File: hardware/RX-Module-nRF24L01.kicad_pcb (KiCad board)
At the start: 2 copper layers, 50 x 22.9 mm, 33 parts, among them J1 Conn_01x03, J10 Conn_01x03, J11 Conn_01x03, J2 Conn_01x03, J3 Conn_01x03, J4 Conn_01x03, J5 Conn_01x03, J6 Conn_01x03, J7 Conn_01x03, J8 Conn_01x03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

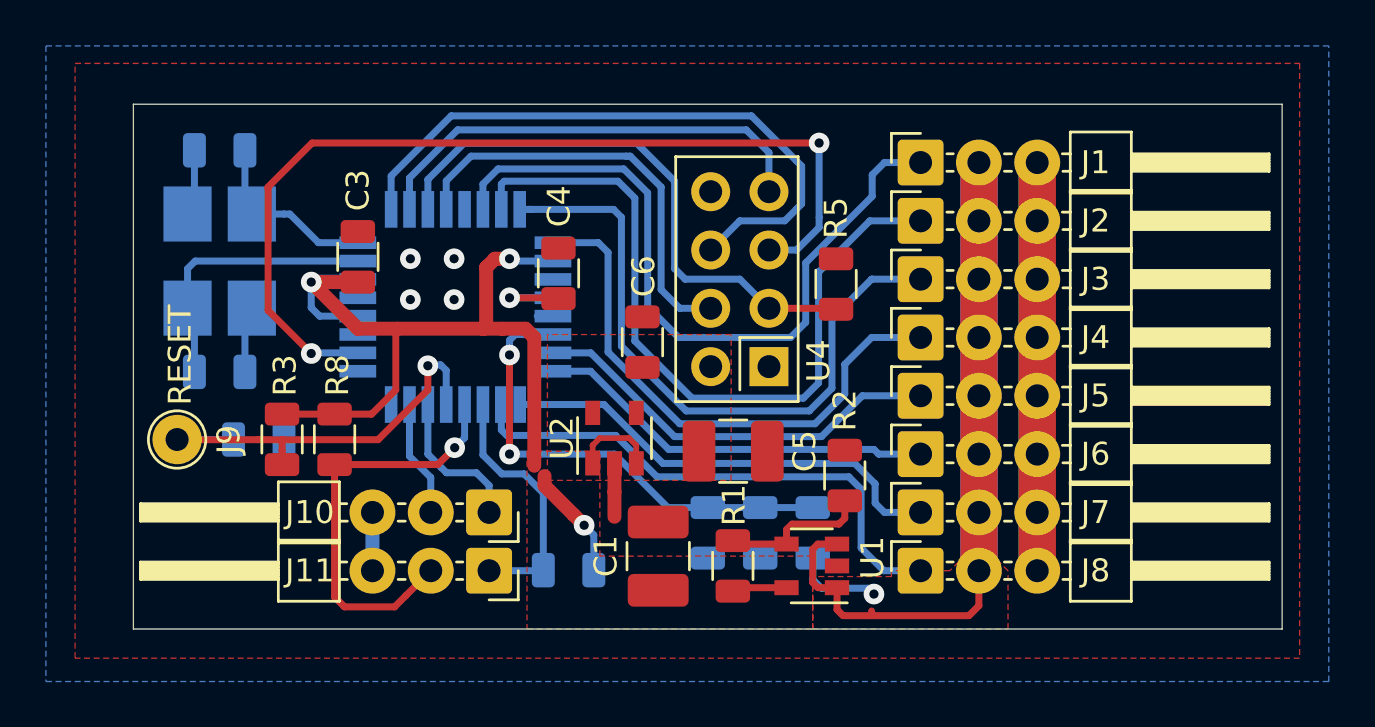
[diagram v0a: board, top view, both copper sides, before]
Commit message: symbol update
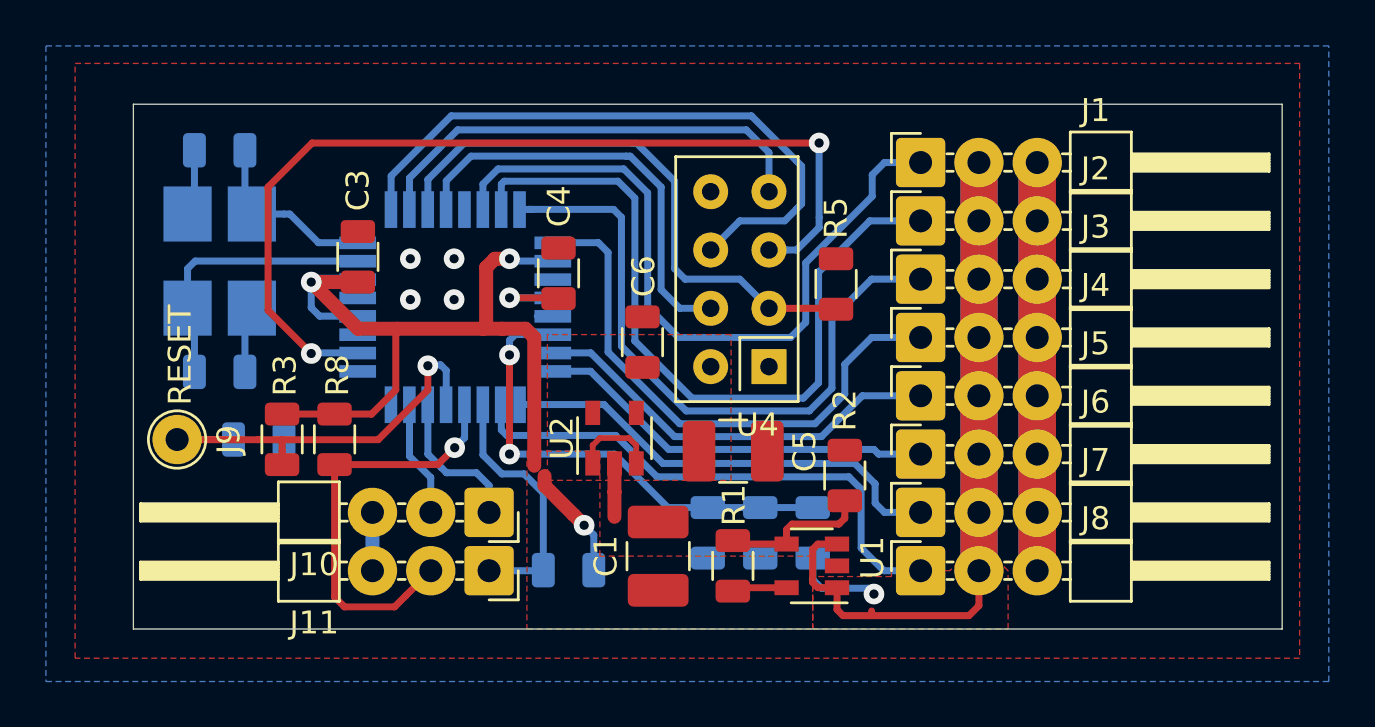
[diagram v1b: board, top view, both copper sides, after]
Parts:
- C1, C5: value 4u7 -> 10u
- J1, J10, J11, J2, J3, J4, J5, J6, J7, J8: footprint obbo-footprints-experimental:PinHeader_3x01_P2.54mm_Horizontal_Pad2mm -> obbo_footprints:PinHeader_3x01_P2.54mm_Horizontal
- R4: value 20k* -> 47k*
- U4: footprint obbo_footprints:nRF24L01-GT24_Breakuot_PinHeader_2x04_Solder -> obbo_footprints:nRF24L01-GT24_Breakout_PinHeader_2x04
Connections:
- net /A7 renamed /VBAT
